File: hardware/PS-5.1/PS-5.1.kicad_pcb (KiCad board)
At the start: 2 copper layers, 199.4 x 199.4 mm, 67 parts, among them CN3 Conn_01x02, CN4 Conn_01x03, CN5 Conn_01x02, J1 PinSocket_02x16_P2.54mm_Verti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, K1 RAYEX-L90, K2 RAYEX-L90, Q1 IRFPE50, Q2 IRFPE50, Q3 IRFPE50, U1 TC4422/ TC4420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

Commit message: modified:   .DS_Store 	modified:   archive/Purchase 20260105.xlsx 	deleted:    hardware/CTL-4.2/CTL-4.2-backups/CTL-4.2-2026-01-07_141653.zip 	deleted:    hardware/CTL-4.2/CTL-4.2-backups/CTL-4.2-2026-01-07_142924.zip 	deleted:    hardware/CTL-4.2/CTL-4.2-backups/CTL-4.2-2026-01-07_143704.zip 	deleted:    hardware/CTL-4.2/CTL-4.2-backups/CTL-4.2-2026-01-07_144240.zip 	deleted:    hardware/CTL-4.2/CTL-4.2-backups/CTL-4.2-2026-01-07_172928.zip 	deleted:    hardware/CTL-4.2/CTL-4.2-backups/CTL-4.2-2026-01-08_104233.zip 	deleted:    hardware/CTL-4.2/CTL-4.2-backups/CTL-4.2-2026-01-08_105414.zip 	deleted:    hardware/CTL-4.2/CTL-4.2-backups/CTL-4.2-2026-01-08_110821.zip 	deleted:    hardware/CTL-4.2/CTL-4.2-backups/CTL-4.2-2026-01-08_113902.zip 	new file:   hardware/CTL-4.2/CTL-4.2-backups/CTL-4.2-2026-01-09_161105.zip 	new file:   hardware/CTL-4.2/CTL-4.2-backups/CTL-4.2-2026-01-09_161607.zip 	new file:   hardware/CTL-4.2/CTL-4.2-backups/CTL-4.2-2026-01-09_162214.zip 	new file:   hardware/CTL-4.2/CTL-4.2-backups/CTL-4.2-2026-01-09_162911.zip 	new file:   hardware/CTL-4.2/CTL-4.2-backups/CTL-4.2-2026-01-09_163538.zip 	new file:   hardware/CTL-4.2/CTL-4.2-backups/CTL-4.2-2026-01-10_175837.zip 	new file:   hardware/CTL-4.2/CTL-4.2-backups/CTL-4.2-2026-01-12_160020.zip 	new file:   hardware/CTL-4.2/CTL-4.2-backups/CTL-4.2-2026-01-12_160649.zip 	new file:   hardware/CTL-4.2/CTL-4.2-backups/CTL-4.2-2026-01-12_161345.zip 	new file:   hardware/CTL-4.2/CTL-4.2-backups/CTL-4.2-2026-01-12_162048.zip 	new file:   hardware/CTL-4.2/CTL-4.2-backups/CTL-4.2-2026-01-12_165205.zip 	new file:   hardware/CTL-4.2/CTL-4.2-backups/CTL-4.2-2026-01-13_144014.zip 	new file:   hardware/CTL-4.2/CTL-4.2-backups/CTL-4.2-2026-01-13_150252.zip 	new file:   hardware/CTL-4.2/CTL-4.2-backups/CTL-4.2-2026-01-13_151249.zip 	new file:   hardware/CTL-4.2/CTL-4.2-backups/CTL-4.2-2026-01-13_151858.zip 	new file:   hardware/CTL-4.2/CTL-4.2-backups/CTL-4.2-2026-01-13_163249.zip 	new file:   hardware/CTL-4.2/CTL-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
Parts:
- moved C10 108.9 mm to (30.2, 119.1)
- moved C11 108.9 mm to (30.2, 100.0)
- moved C12 108.9 mm to (30.2, 138.1)
- moved C6 108.9 mm to (115.6, 76.3)
- moved C7 108.9 mm to (30.2, 52.4)
- moved C8 108.9 mm to (30.2, 33.3)
- moved C9 108.9 mm to (30.2, 71.4)
- moved CN-1-1 108.9 mm to (195.9, 194.8)
- moved CN-1-2 108.9 mm to (195.9, 211.9)
- moved CR1 108.9 mm to (128.9, 39.4)
- moved CR2 108.9 mm to (145.4, 39.4)
- moved D4 108.9 mm to (188.0, 62.2)
- moved D5 108.9 mm to (172.7, 49.5)
- moved D6 108.9 mm to (188.0, 55.9)
- moved D7 108.9 mm to (180.7, 177.5)
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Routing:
- net /PWM: track 53.5 -> 51.6 mm
- net Net-(R1-Pad2): track 108.3 -> 107.1 mm
- net GND: vias 0 -> 5

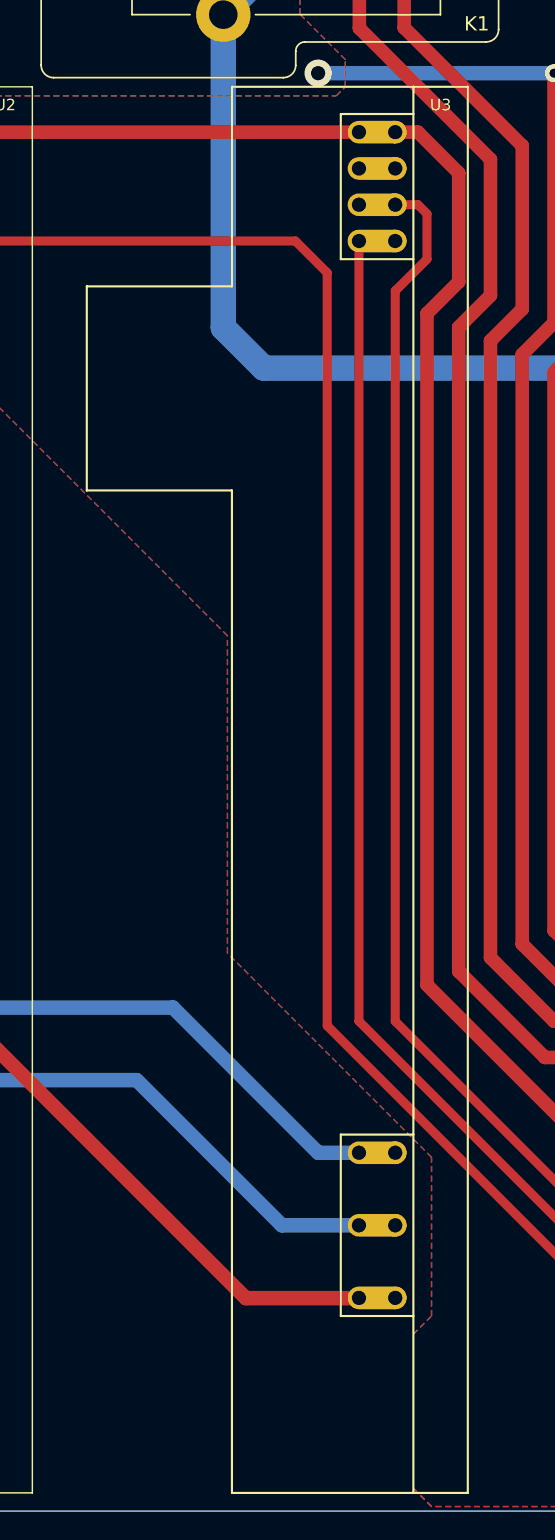
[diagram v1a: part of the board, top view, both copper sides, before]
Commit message: modified:   .DS_Store 	new file:   CAD/FR_TEST.dxf 	modified:   Ferrite Transformer Calculation.xlsx 	new file:   archive/PR_ 0201_2026.docx 	modified:   archive/Purchase 20260105.xlsx 	new file:   archive/Purchase 20260209.zip 	new file:   archive/Purchase 20260209/Invoice | Tokopedia 1.pdf 	new file:   archive/Purchase 20260209/Invoice | Tokopedia 2.pdf 	new file:   archive/Purchase 20260209/Invoice | Tokopedia 3.pdf 	new file:   archive/Purchase 20260209/Invoice | Tokopedia 4.pdf 	new file:   archive/Purchase 20260209/Invoice | Tokopedia 5.pdf 	new file:   archive/Purchase_20260109_0924.jpg 	new file:   archive/Purchase_20260209_0924.xlsx 	new file:   archive/R parallel.xlsx 	modified:   firmware/ESP32-S3 PWM/include/config.h 	modified:   firmware/ESP32-S3 PWM/include/hardware_control.h 	modified:   firmware/ESP32-S3 PWM/platformio.ini 	modified:   firmware/ESP32-S3 PWM/src/hardware_control.cpp 	modified:   firmware/ESP32-S3 PWM/src/main.cpp 	new file:   hardware/CTL-4.3/CTL-4.3-backups/CTL-4.3-2026-02-11_163805.zip 	new file:   hardware/CTL-4.3/CTL-4.3-backups/CTL-4.3-2026-02-13_145455.zip 	new file:   hardware/CTL-4.3/CTL-4.3-backups/CTL-4.3-2026-02-13_163249.zip 	new file:   hardware/CTL-4.3/CTL-4.3-backups/CTL-4.3-2026-02-18_163417.zip 	new file:   hardware/CTL-4.3/CTL-4.3-backups/CTL-4.3-2026-02-19_083102.zip 	new file:   hardware/CTL-4.3/CTL-4.3-backups/CTL-4.3-2026-03-04_102408.zip 	modified:   hardware/CTL-4.3/fp-info-cache 	new file:   hardware/CTL-5.0/CTL-4.3-backups/CTL-4.3-2026-01-19_105947.zip 	new file:   hardware/CTL-5.0/CTL-4.3-backups/CTL-4.3-2026-01-19_110601.zip 	new file:   hardware/CTL-5.0/CTL-4.3-backups/CTL-4.3-2026-01-19_111804.zip 	new file:   hardware/CTL-5.0/CTL-4.3-backups/CTL-4.3-2026-01-19_113721.zip 	new file:   hardware/CTL-5.0/CTL-4.3-backups/CTL-4.3-2026-01-19_164107.zip 	new file:   hardware/CTL-5.0/CTL-4.3-backups/CTL-4.3-2026-01-20_112913.zip 	new file:   hardware/CTL-5.0/CTL-4.3-backups/CTL-4.3-2026-02-11_163805.zip 	new file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
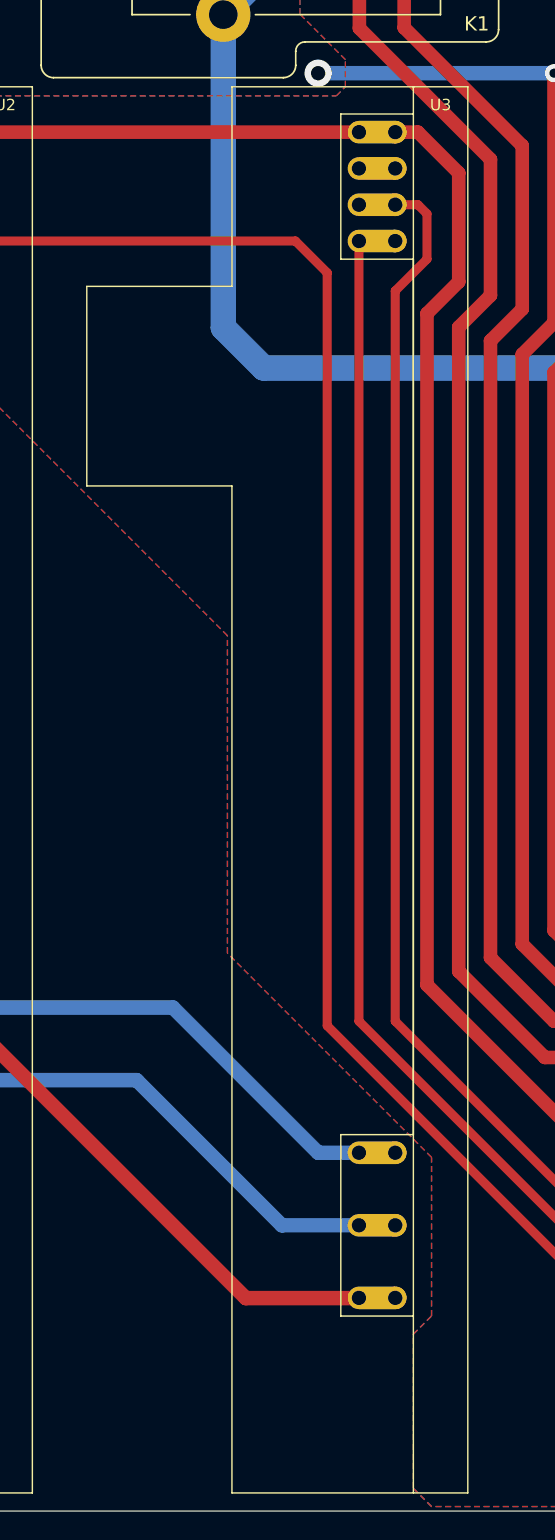
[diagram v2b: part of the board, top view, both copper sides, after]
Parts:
- U3: footprint Custom:ESU-MSD-1.0 -> Custom:ESU-REM-4.0
